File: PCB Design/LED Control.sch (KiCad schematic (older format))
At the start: 25 parts, among them J1 5V 5A Power, J2 TO WS2812B LED STRIP, J3 Conn_01x03, SW1 SW_Push_Dual

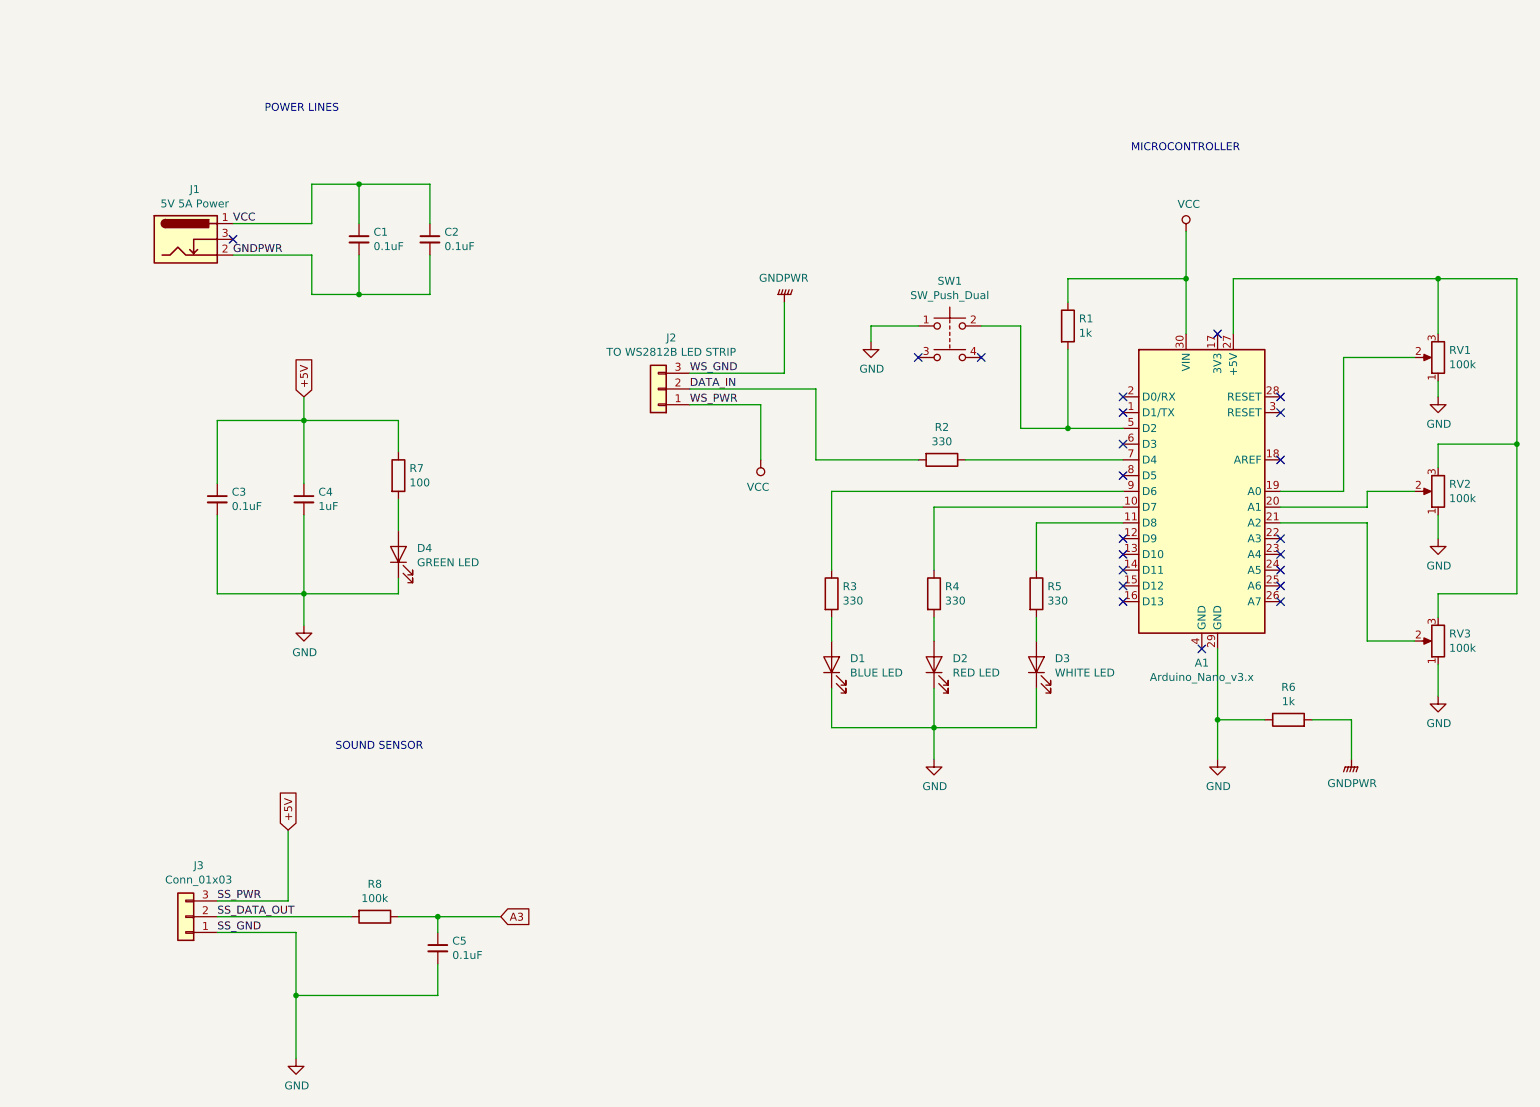
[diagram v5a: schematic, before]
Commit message: pull up/down resistors added
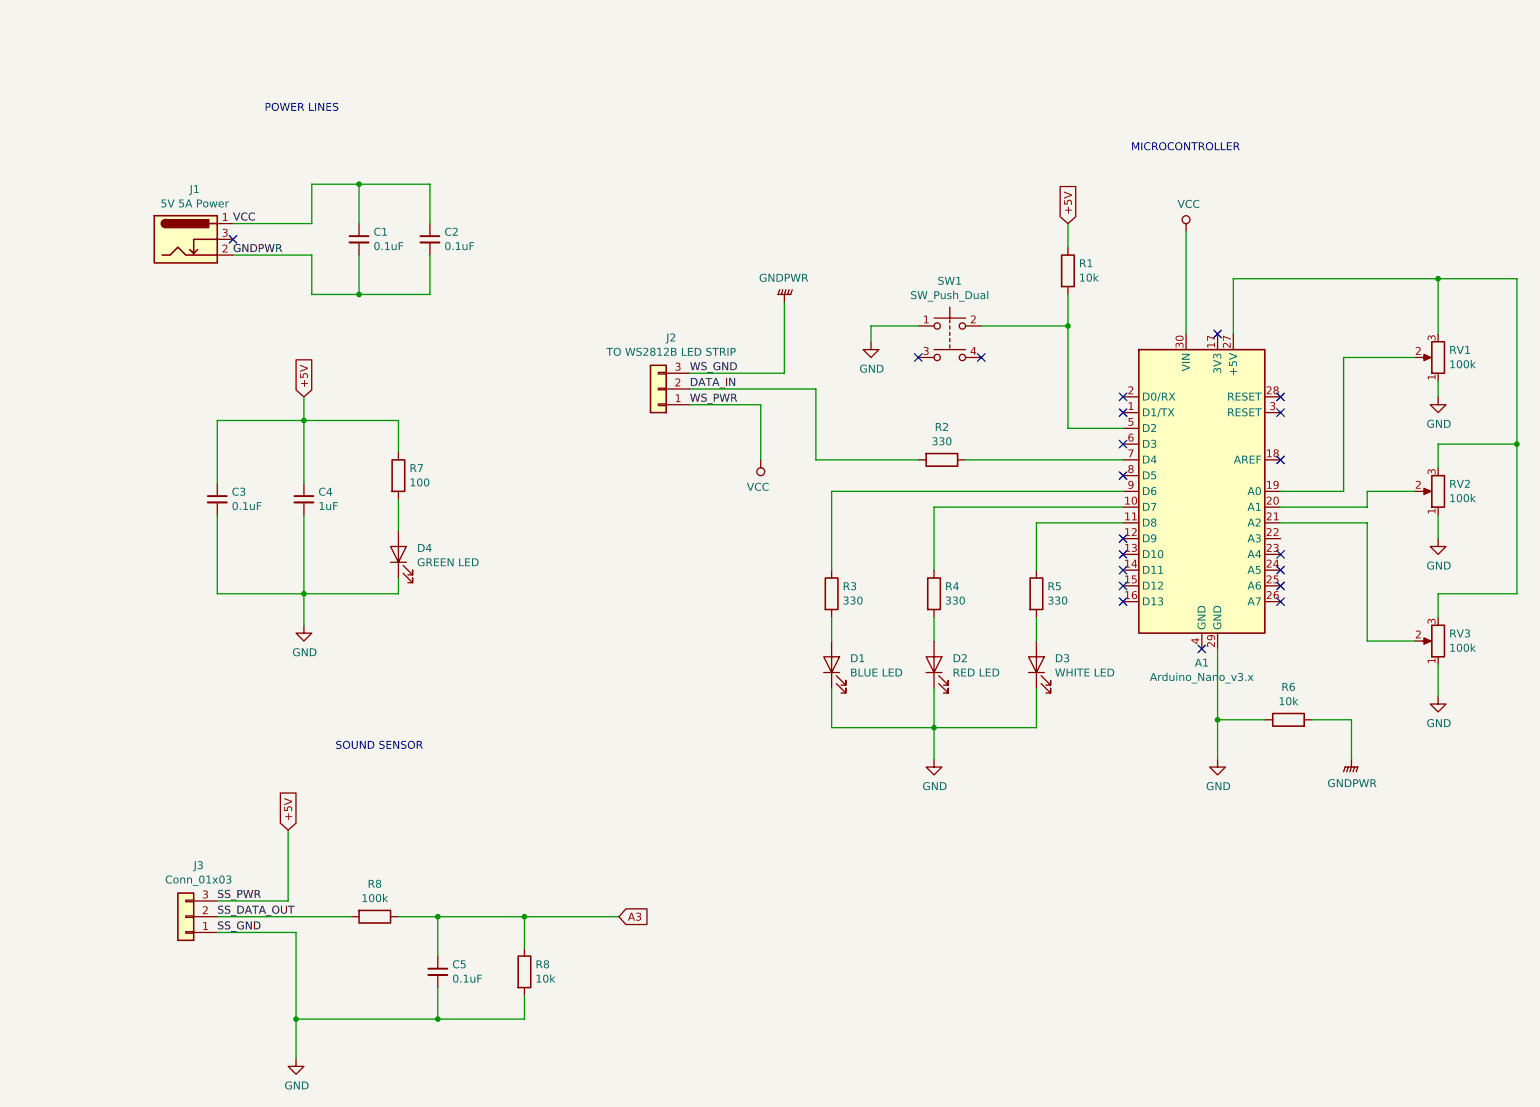
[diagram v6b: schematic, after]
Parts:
- added R8: 10k, Resistor_SMD:R_0805_2012Metric, symbol Device:R
- R1, R6: value 1k -> 10k; LCSC C17513 -> C17414
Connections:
- net +5V: now also R1.1
- net A3: now also R8.1
- net GND: now also R8.2
- net VCC: no longer R1.1
- no-connect marks 22 -> 21
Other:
- moved on the sheet: C5, R1
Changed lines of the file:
@@
 	6700 5250 6700 5050
 Wire Wire Line
-	8300 1900 8300 2200
-Wire Wire Line
-	7900 3150 7550 3150
-Wire Wire Line
-	8300 2200 7550 2200
-Connection ~ 8300 2200
-Wire Wire Line
-	8300 2200 8300 2550
-Wire Wire Line
-	7000 2500 7250 2500
-Wire Wire Line
-	7250 2500 7250 3150
-Wire Wire Line
-	7250 3150 7550 3150
-Connection ~ 7550 3150
-Wire Wire Line
-	7550 2200 7550 2350
-Wire Wire Line
-	7550 3150 7550 2650
+	7550 1850 7550 2000
 $Comp
 L Device:R R1
 U 1 1 5DBEB19F
-P 7550 2500
-F 0 "R1" H 7620 2546 50  0000 L CNN
-F 1 "1k" H 7620 2455 50  0000 L CNN
-F 2 "Resistor_SMD:R_0805_2012Metric" V 7480 2500 50  0001 C CNN
-F 3 "~" H 7550 2500 50  0001 C CNN
-F 4 "C17513" H 7550 2500 50  0001 C CNN "LCSC"
-	1    7550 2500
+P 7550 2150
+F 0 "R1" H 7620 2196 50  0000 L CNN
+F 1 "10k" H 7620 2105 50  0000 L CNN
+F 2 "Resistor_SMD:R_0805_2012Metric" V 7480 2150 50  0001 C CNN
+F 3 "~" H 7550 2150 50  0001 C CNN
+F 4 "C17414" H 7550 2150 50  0001 C CNN "LCSC"
+	1    7550 2150
 	1    0    0    -1
 $EndComp
@@
 P 8950 5000
 F 0 "R6" V 9157 5000 50  0000 C CNN
-F 1 "1k" V 9066 5000 50  0000 C CNN
+F 1 "10k" V 9066 5000 50  0000 C CNN
 F 2 "Resistor_SMD:R_0805_2012Metric" V 8880 5000 50  0001 C CNN
 F 3 "~" H 8950 5000 50  0001 C CNN
-F 4 "C17513" V 8950 5000 50  0001 C CNN "LCSC"
+F 4 "C17414" V 8950 5000 50  0001 C CNN "LCSC"
 	1    8950 5000
 	0    -1   -1   0
@@
 	2150 6350 2650 6350
 Wire Wire Line
-	2650 6350 2650 6750
-Wire Wire Line
-	3550 6750 2650 6750
-Connection ~ 2650 6750
-Wire Wire Line
-	2650 6750 2650 7150
+	3550 6900 2650 6900
 Wire Wire Line
 	3300 6250 3550 6250
-Wire Wire Line
-	3550 6250 3550 6350
 $Comp
 L Device:R R8
@@
 Wire Wire Line
 	3000 6250 2150 6250
-Wire Wire Line
-	3550 6250 3950 6250
 Connection ~ 3550 6250
-Text GLabel 3950 6250 2    50   Input ~ 0
+Text GLabel 4700 6250 2    50   Input ~ 0
 A3
 Text Label 2150 6250 0    50   ~ 0
@@
 NoConn ~ 8900 4050
 NoConn ~ 8900 3950
-NoConn ~ 8900 3850
 $Comp
 L Device:C_Small C5
 U 1 1 5E4E4C59
-P 3550 6450
-F 0 "C5" H 3642 6496 50  0000 L CNN
-F 1 "0.1uF" H 3642 6405 50  0000 L CNN
-F 2 "Capacitor_THT:C_Disc_D3.4mm_W2.1mm_P2.50mm" H 3550 6450 50  0001 C CNN
-F 3 "~" H 3550 6450 50  0001 C CNN
-	1    3550 6450
-	1    0    0    -1
-$EndComp
-Wire Wire Line
-	3550 6550 3550 6750
+P 3550 6600
+F 0 "C5" H 3642 6646 50  0000 L CNN
+F 1 "0.1uF" H 3642 6555 50  0000 L CNN
+F 2 "Capacitor_THT:C_Disc_D3.4mm_W2.1mm_P2.50mm" H 3550 6600 50  0001 C CNN
+F 3 "~" H 3550 6600 50  0001 C CNN
+	1    3550 6600
+	1    0    0    -1
+$EndComp
+Wire Wire Line
+	3550 6700 3550 6900
 $Comp
 L Device:C_Small C1
@@
 	1    0    0    -1
 $EndComp
+Wire Wire Line
+	8300 1900 8300 2550
+Text GLabel 7550 1850 1    50   Input ~ 0
++5V
+Wire Wire Line
+	2650 6350 2650 6900
+Connection ~ 2650 6900
+Wire Wire Line
+	2650 6900 2650 7150
+$Comp
+L Device:R R8
+U 1 1 5E43894A
+P 4100 6600
+F 0 "R8" H 4170 6646 50  0000 L CNN
+F 1 "10k" H 4170 6555 50  0000 L CNN
+F 2 "Resistor_SMD:R_0805_2012Metric" V 4030 6600 50  0001 C CNN
+F 3 "~" H 4100 6600 50  0001 C CNN
+F 4 "C17414" H 4100 6600 50  0001 C CNN "LCSC"
+	1    4100 6600
+	1    0    0    -1
+$EndComp
+Wire Wire Line
+	4100 6450 4100 6250
+Wire Wire Line
+	3550 6250 4100 6250
+Connection ~ 4100 6250
+Wire Wire Line
+	4100 6250 4700 6250
+Wire Wire Line
+	4100 6750 4100 6900
+Wire Wire Line
+	4100 6900 3550 6900
+Connection ~ 3550 6900
+Wire Wire Line
+	3550 6250 3550 6500
+Wire Wire Line
+	7900 3150 7550 3150
+Wire Wire Line
+	7550 3150 7550 2500
+Wire Wire Line
+	7000 2500 7550 2500
+Wire Wire Line
+	7550 2300 7550 2500
+Connection ~ 7550 2500
 $EndSCHEMATC

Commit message: pcb layout created
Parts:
- J2: footprint Connector_JST:JST_PH_S3B-PH-K_1x03_P2.00mm_Horizontal -> TerminalBlock_Phoenix:TerminalBlock_Phoenix_MPT-0,5-3-2.54_1x03_P2.54mm_Horizontal
- J3: value Conn_01x03 -> Sound Sensor
- R8: footprint Resistor_THT:R_Axial_DIN0207_L6.3mm_D2.5mm_P10.16mm_Horizontal -> Resistor_SMD:R_0805_2012Metric; LCSC (none) -> C17407
- renumbered R8 to R9
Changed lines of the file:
@@
 F 0 "J2" H 4868 2575 50  0000 C CNN
 F 1 "TO WS2812B LED STRIP" H 4868 2666 50  0000 C CNN
-F 2 "Connector_JST:JST_PH_S3B-PH-K_1x03_P2.00mm_Horizontal" H 4950 2900 50  0001 C CNN
+F 2 "TerminalBlock_Phoenix:TerminalBlock_Phoenix_MPT-0,5-3-2.54_1x03_P2.54mm_Horizontal" H 4950 2900 50  0001 C CNN
 F 3 "~" H 4950 2900 50  0001 C CNN
 	1    4950 2900
@@
 P 1950 6250
 F 0 "J3" H 1868 5925 50  0000 C CNN
-F 1 "Conn_01x03" H 1868 6016 50  0000 C CNN
+F 1 "Sound Sensor" H 1868 6016 50  0000 C CNN
 F 2 "TerminalBlock_Phoenix:TerminalBlock_Phoenix_MPT-0,5-3-2.54_1x03_P2.54mm_Horizontal" H 1950 6250 50  0001 C CNN
 F 3 "~" H 1950 6250 50  0001 C CNN
@@
 F 0 "R8" V 2943 6250 50  0000 C CNN
 F 1 "100k" V 3034 6250 50  0000 C CNN
-F 2 "Resistor_THT:R_Axial_DIN0207_L6.3mm_D2.5mm_P10.16mm_Horizontal" V 3080 6250 50  0001 C CNN
+F 2 "Resistor_SMD:R_0805_2012Metric" V 3080 6250 50  0001 C CNN
 F 3 "~" H 3150 6250 50  0001 C CNN
+F 4 "C17407" V 3150 6250 50  0001 C CNN "LCSC"
 	1    3150 6250
 	0    1    1    0
@@
 	2650 6900 2650 7150
 $Comp
-L Device:R R8
+L Device:R R9
 U 1 1 5E43894A
 P 4100 6600
-F 0 "R8" H 4170 6646 50  0000 L CNN
+F 0 "R9" H 4170 6646 50  0000 L CNN
 F 1 "10k" H 4170 6555 50  0000 L CNN
 F 2 "Resistor_SMD:R_0805_2012Metric" V 4030 6600 50  0001 C CNN

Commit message: pcb size made 60x60
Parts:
- R8: footprint Resistor_SMD:R_0805_2012Metric -> Resistor_THT:R_Axial_DIN0204_L3.6mm_D1.6mm_P5.08mm_Horizontal
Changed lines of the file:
@@
 F 0 "R8" V 2943 6250 50  0000 C CNN
 F 1 "100k" V 3034 6250 50  0000 C CNN
-F 2 "Resistor_SMD:R_0805_2012Metric" V 3080 6250 50  0001 C CNN
+F 2 "Resistor_THT:R_Axial_DIN0204_L3.6mm_D1.6mm_P5.08mm_Horizontal" V 3080 6250 50  0001 C CNN
 F 3 "~" H 3150 6250 50  0001 C CNN
 F 4 "C17407" V 3150 6250 50  0001 C CNN "LCSC"
